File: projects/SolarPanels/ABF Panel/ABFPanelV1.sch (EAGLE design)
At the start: 43 parts

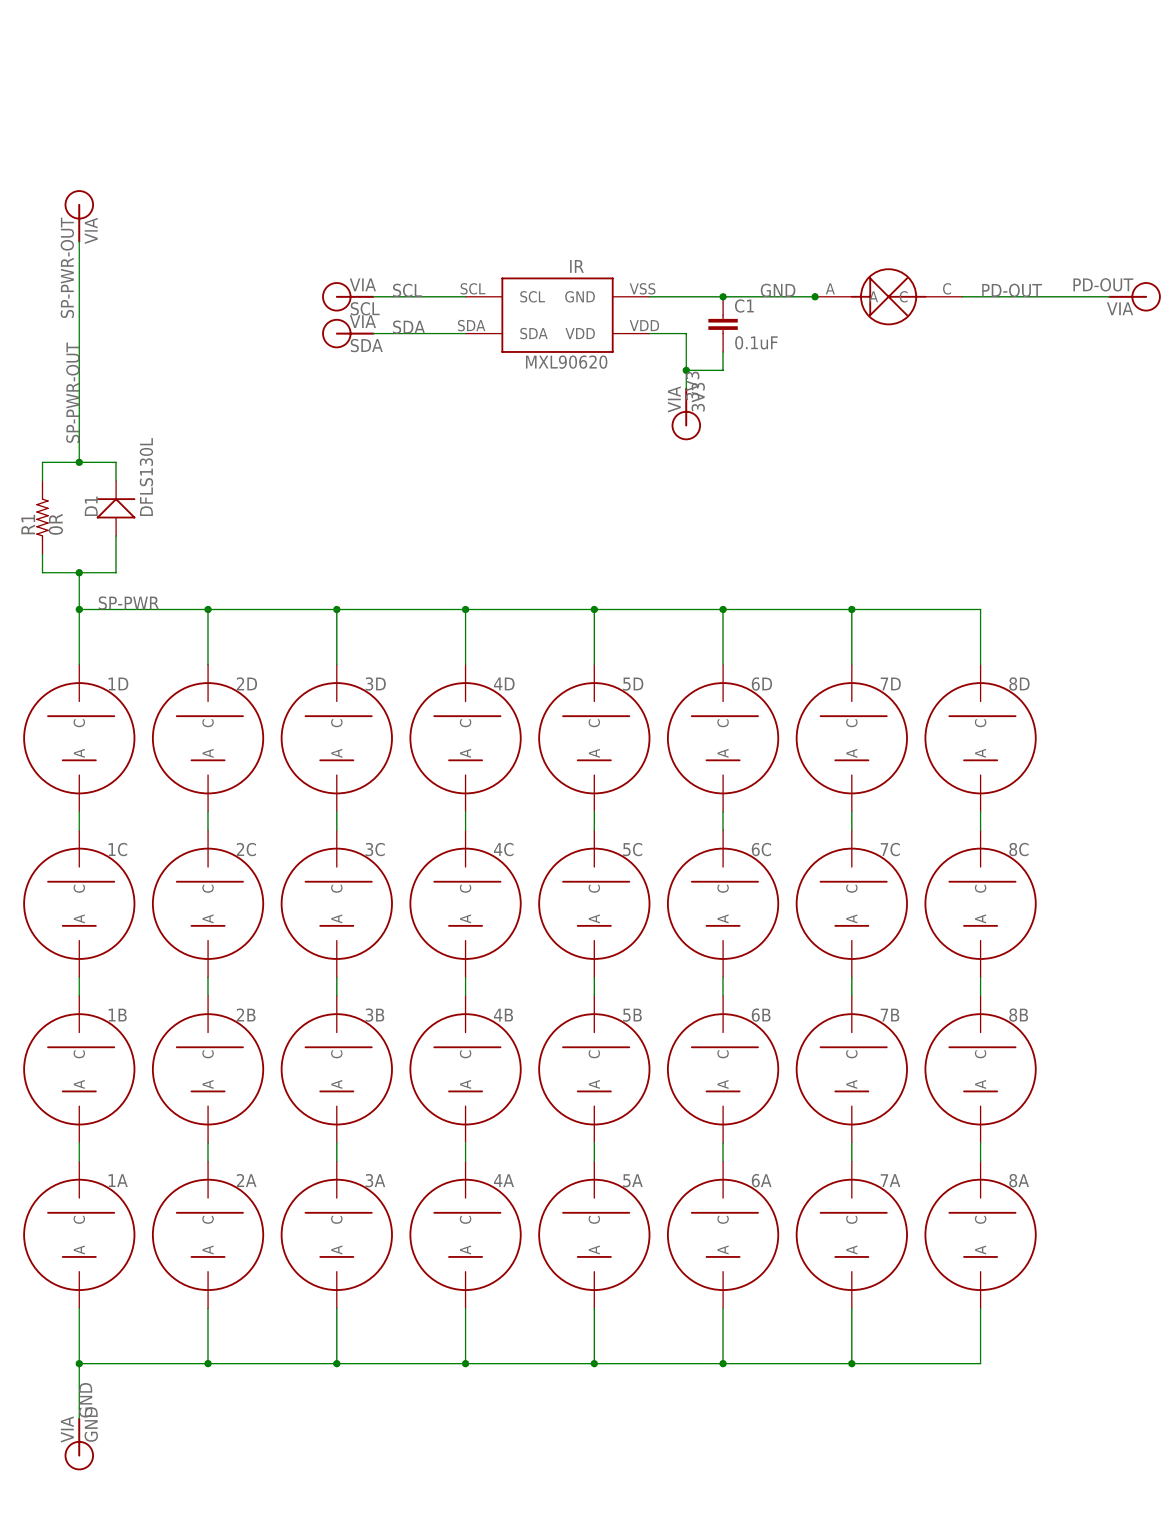
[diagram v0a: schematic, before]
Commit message: Initial commit of ABFPanelV1 and cosmetic changes to SidePanelV5 (change square vias to circular).
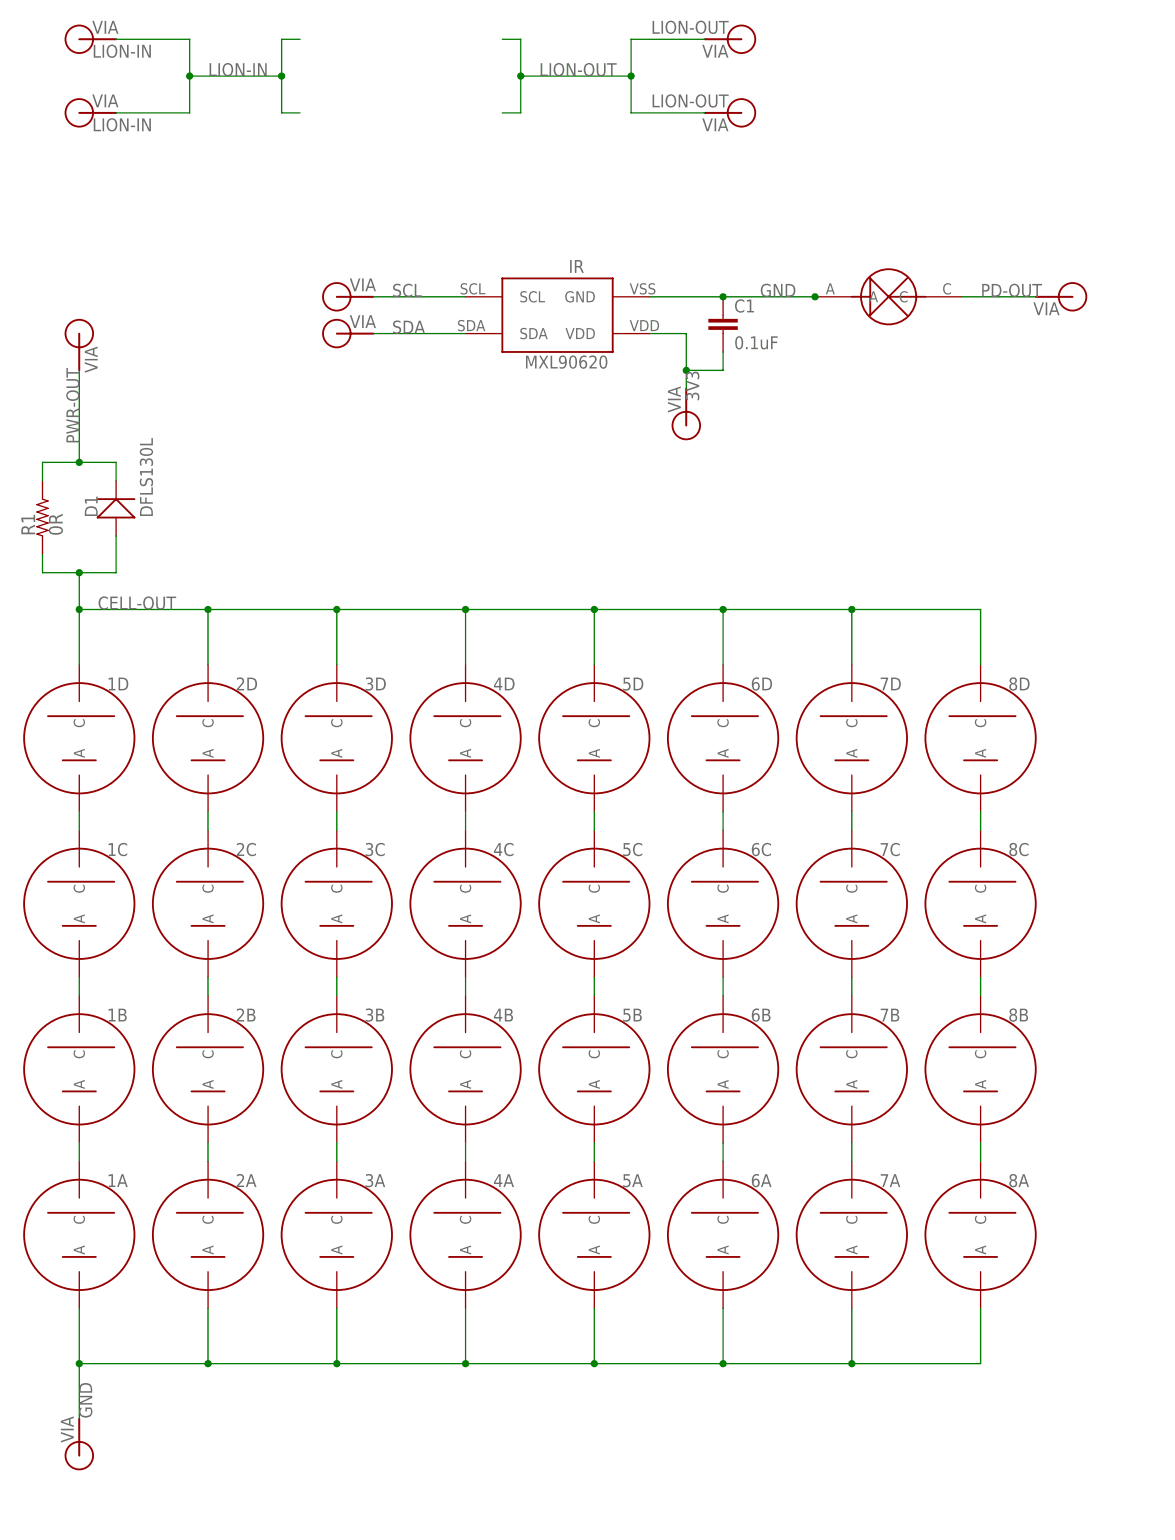
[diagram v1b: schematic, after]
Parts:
- added V1, V2: LION-IN, BrownSpaceEngineering:VIA-60MIL
- added V3, V4: LION-OUT, BrownSpaceEngineering:VIA-60MIL
- 3V3: value 3V3 -> (none)
- GND: value GND -> (none)
- PD-OUT: value PD-OUT -> (none)
- PWR-OUT: value SP-PWR-OUT -> (none)
- SCL: value SCL -> (none)
- SDA: value SDA -> (none)
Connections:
- net SP-PWR renamed CELL-OUT
- net SP-PWR-OUT renamed PWR-OUT
- new net LION-IN: V1.P$1, V2.P$1
- new net LION-OUT: V3.P$1, V4.P$1
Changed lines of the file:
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@@
 <part name="8B" library="BrownSpaceEngineering" deviceset="SOLARCELLV3" device=""/>
 <part name="8A" library="BrownSpaceEngineering" deviceset="SOLARCELLV3" device=""/>
-<part name="SCL" library="BrownSpaceEngineering" deviceset="VIA" device="-60MIL" value="SCL"/>
-<part name="SDA" library="BrownSpaceEngineering" deviceset="VIA" device="-60MIL" value="SDA"/>
-<part name="PD-OUT" library="BrownSpaceEngineering" deviceset="VIA" device="-60MIL" value="PD-OUT"/>
-<part name="3V3" library="BrownSpaceEngineering" deviceset="VIA" device="-60MIL" value="3V3"/>
-<part name="PWR-OUT" library="BrownSpaceEngineering" deviceset="VIA" device="-60MIL" value="SP-PWR-OUT"/>
-<part name="GND" library="BrownSpaceEngineering" deviceset="VIA" device="-60MIL" value="GND"/>
+<part name="SCL" library="BrownSpaceEngineering" deviceset="VIA" device="-60MIL"/>
+<part name="SDA" library="BrownSpaceEngineering" deviceset="VIA" device="-60MIL"/>
+<part name="PD-OUT" library="BrownSpaceEngineering" deviceset="VIA" device="-60MIL"/>
+<part name="3V3" library="BrownSpaceEngineering" deviceset="VIA" device="-60MIL"/>
+<part name="PWR-OUT" library="BrownSpaceEngineering" deviceset="VIA" device="-60MIL"/>
+<part name="GND" library="BrownSpaceEngineering" deviceset="VIA" device="-60MIL"/>
 <part name="D1" library="BrownSpaceEngineering" deviceset="DFLS130L" device="" value="DFLS130L"/>
 <part name="R1" library="BrownSpaceEngineering" deviceset="RES" device="1210" value="0R"/>
+<part name="V1" library="BrownSpaceEngineering" deviceset="VIA" device="-60MIL" value="LION-IN"/>
+<part name="V2" library="BrownSpaceEngineering" deviceset="VIA" device="-60MIL" value="LION-IN"/>
+<part name="V3" library="BrownSpaceEngineering" deviceset="VIA" device="-60MIL" value="LION-OUT"/>
+<part name="V4" library="BrownSpaceEngineering" deviceset="VIA" device="-60MIL" value="LION-OUT"/>
 </parts>
 <sheets>
@@
 <instance part="SCL" gate="G$1" x="-109.22" y="106.68"/>
 <instance part="SDA" gate="G$1" x="-109.22" y="101.6"/>
-<instance part="PD-OUT" gate="G$1" x="2.54" y="106.68" rot="R180"/>
+<instance part="PD-OUT" gate="G$1" x="-7.62" y="106.68" rot="R180"/>
 <instance part="3V3" gate="G$1" x="-60.96" y="88.9" rot="R90"/>
-<instance part="PWR-OUT" gate="G$1" x="-144.78" y="119.38" smashed="yes" rot="R270">
-<attribute name="VALUE" x="-147.32" y="117.602" size="1.778" layer="96" rot="R270"/>
+<instance part="PWR-OUT" gate="G$1" x="-144.78" y="101.6" smashed="yes" rot="R270">
+<attribute name="VALUE" x="-147.32" y="99.822" size="1.778" layer="96" rot="R270"/>
 </instance>
 <instance part="GND" gate="G$1" x="-144.78" y="-53.34" rot="R90"/>
 <instance part="D1" gate="G$1" x="-139.7" y="76.2" rot="R90"/>
 <instance part="R1" gate="R$1" x="-149.86" y="76.2" rot="R90"/>
+<instance part="V1" gate="G$1" x="-144.78" y="142.24"/>
+<instance part="V2" gate="G$1" x="-144.78" y="132.08"/>
+<instance part="V3" gate="G$1" x="-53.34" y="142.24" rot="R180"/>
+<instance part="V4" gate="G$1" x="-53.34" y="132.08" rot="R180"/>
 </instances>
 <busses>
@@
 <segment>
 <pinref part="PD" gate="G$1" pin="C"/>
-<wire x1="-22.86" y1="106.68" x2="-2.54" y2="106.68" width="0.1524" layer="91"/>
+<wire x1="-22.86" y1="106.68" x2="-12.7" y2="106.68" width="0.1524" layer="91"/>
 <label x="-20.32" y="106.68" size="1.778" layer="95"/>
 <pinref part="PD-OUT" gate="G$1" pin="P$1"/>
@@
 </segment>
 </net>
-<net name="SP-PWR" class="0">
+<net name="CELL-OUT" class="0">
 <segment>
 <pinref part="7D" gate="G$1" pin="C"/>
@@
 </segment>
 </net>
-<net name="SP-PWR-OUT" class="0">
+<net name="PWR-OUT" class="0">
 <segment>
 <pinref part="R1" gate="R$1" pin="2"/>
@@
 <pinref part="PWR-OUT" gate="G$1" pin="P$1"/>
 <wire x1="-144.78" y1="83.82" x2="-149.86" y2="83.82" width="0.1524" layer="91"/>
-<wire x1="-144.78" y1="83.82" x2="-144.78" y2="114.3" width="0.1524" layer="91"/>
+<wire x1="-144.78" y1="83.82" x2="-144.78" y2="96.52" width="0.1524" layer="91"/>
 <junction x="-144.78" y="83.82"/>
 <label x="-144.78" y="86.36" size="1.778" layer="95" rot="R90"/>
 </segment>
 </net>
+<net name="LION-IN" class="0">
+<segment>
+<pinref part="V1" gate="G$1" pin="P$1"/>
+<wire x1="-139.7" y1="142.24" x2="-129.54" y2="142.24" width="0.1524" layer="91"/>
+<pinref part="V2" gate="G$1" pin="P$1"/>
+<wire x1="-139.7" y1="132.08" x2="-129.54" y2="132.08" width="0.1524" layer="91"/>
+<wire x1="-129.54" y1="132.08" x2="-129.54" y2="137.16" width="0.1524" layer="91"/>
+<wire x1="-129.54" y1="137.16" x2="-129.54" y2="142.24" width="0.1524" layer="91"/>
+<wire x1="-129.54" y1="137.16" x2="-116.84" y2="137.16" width="0.1524" layer="91"/>
+<junction x="-129.54" y="137.16"/>
+<wire x1="-116.84" y1="137.16" x2="-116.84" y2="142.24" width="0.1524" layer="91"/>
+<wire x1="-116.84" y1="142.24" x2="-114.3" y2="142.24" width="0.1524" layer="91"/>
+<wire x1="-116.84" y1="137.16" x2="-116.84" y2="132.08" width="0.1524" layer="91"/>
+<junction x="-116.84" y="137.16"/>
+<wire x1="-116.84" y1="132.08" x2="-114.3" y2="132.08" width="0.1524" layer="91"/>
+<label x="-127" y="137.16" size="1.778" layer="95"/>
+</segment>
+</net>
+<net name="LION-OUT" class="0">
+<segment>
+<pinref part="V3" gate="G$1" pin="P$1"/>
+<wire x1="-58.42" y1="142.24" x2="-68.58" y2="142.24" width="0.1524" layer="91"/>
+<wire x1="-68.58" y1="142.24" x2="-68.58" y2="137.16" width="0.1524" layer="91"/>
+<pinref part="V4" gate="G$1" pin="P$1"/>
+<wire x1="-68.58" y1="137.16" x2="-68.58" y2="132.08" width="0.1524" layer="91"/>
+<wire x1="-68.58" y1="132.08" x2="-58.42" y2="132.08" width="0.1524" layer="91"/>
+<wire x1="-68.58" y1="137.16" x2="-83.82" y2="137.16" width="0.1524" layer="91"/>
+<junction x="-68.58" y="137.16"/>
+<wire x1="-83.82" y1="137.16" x2="-83.82" y2="142.24" width="0.1524" layer="91"/>
+<wire x1="-83.82" y1="142.24" x2="-86.36" y2="142.24" width="0.1524" layer="91"/>
+<wire x1="-83.82" y1="137.16" x2="-83.82" y2="132.08" width="0.1524" layer="91"/>
+<junction x="-83.82" y="137.16"/>
+<wire x1="-83.82" y1="132.08" x2="-86.36" y2="132.08" width="0.1524" layer="91"/>
+<label x="-81.28" y="137.16" size="1.778" layer="95"/>
+</segment>
+</net>
